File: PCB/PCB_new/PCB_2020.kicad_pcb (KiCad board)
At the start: 2 copper layers, 94 x 98.4 mm, 26 parts, among them IC1 LM358N, J1 TI_CONN, J10 SERVO_CONN, J11 MC_CONN, Q1 220mA/50V/3.5Ω, Q2 100V/17A, Q3 100V/17A, Q4 100V/17A, Q5 100V/17A, Q6 100V/17A

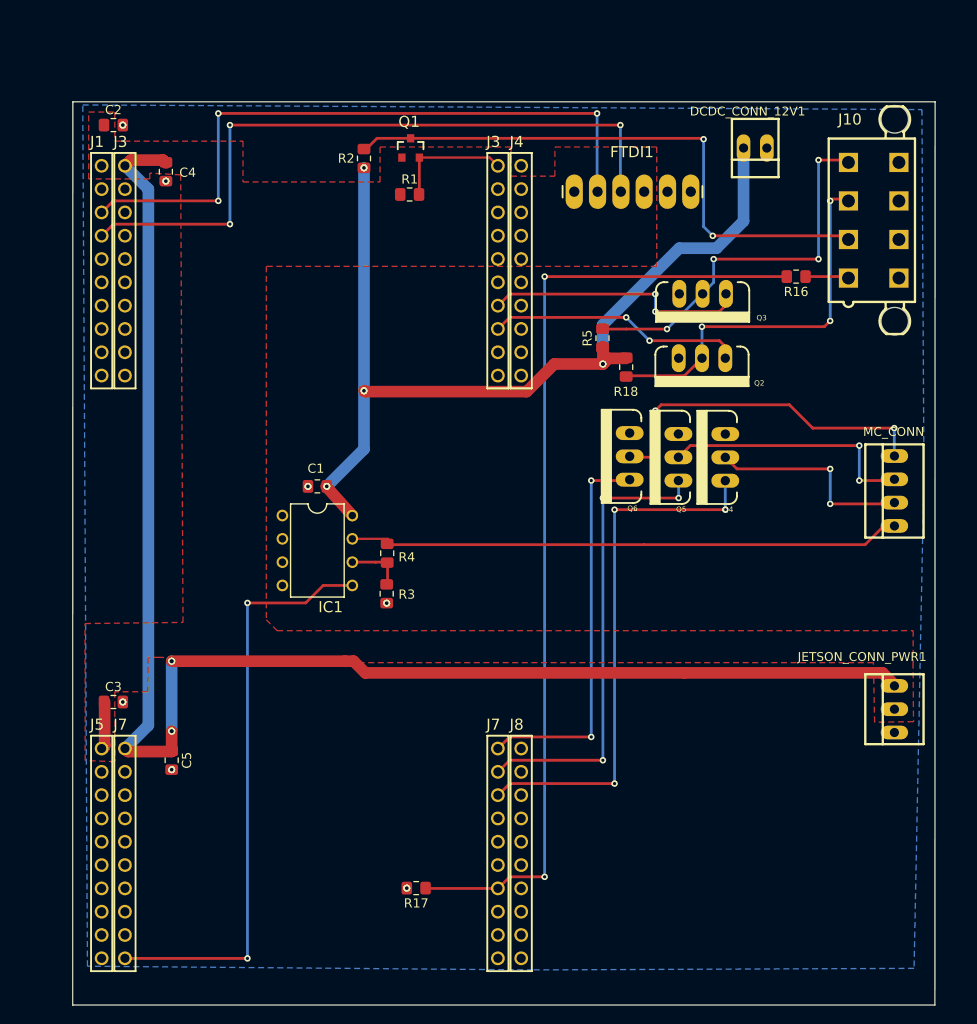
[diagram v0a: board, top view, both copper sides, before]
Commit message: new pcb design (still no braking signals)
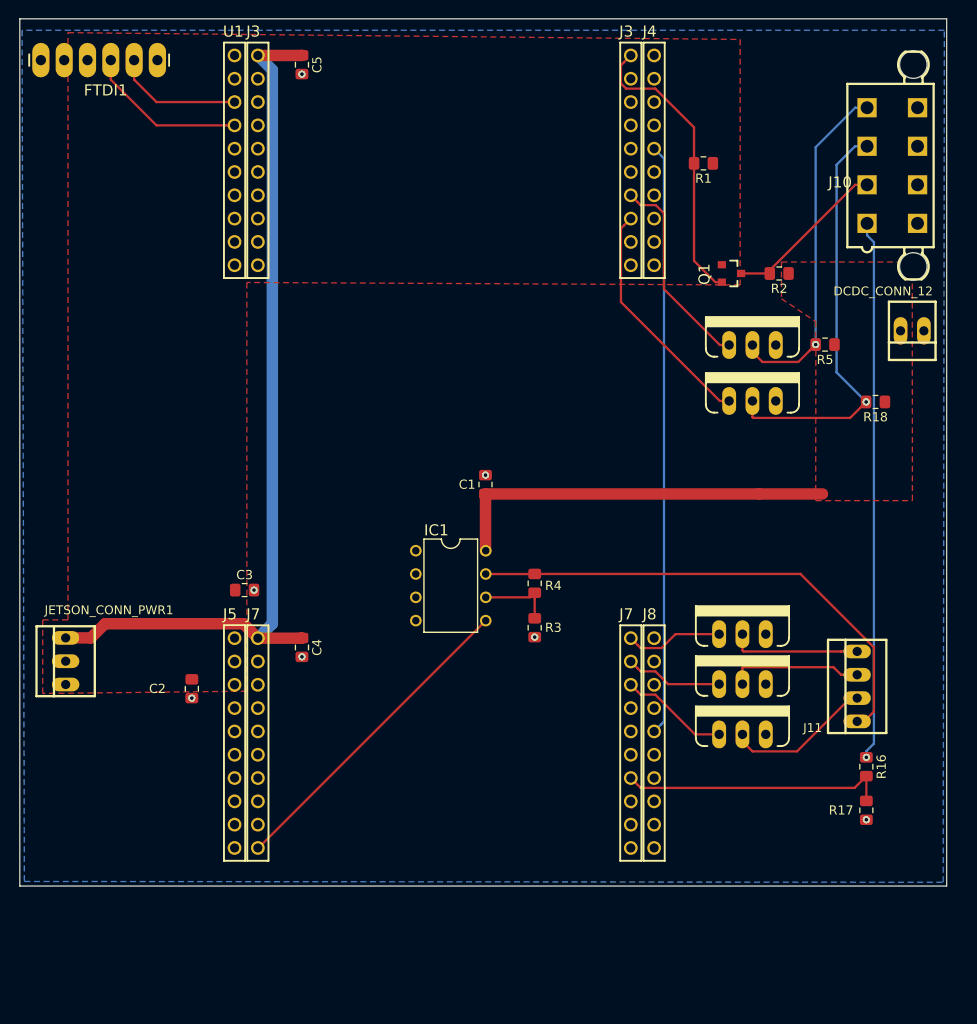
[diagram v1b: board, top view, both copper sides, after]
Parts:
- removed DCDC_CONN_12V1: 22-23-2021, Drivetrain_control:22-23-2021
- removed J1: TI_CONN, Drivetrain_control:TI_Footprint
- added DCDC_CONN_12: 22-23-2021, Drivetrain_control:22-23-2021, F.Cu at (193.0, 80.8)
- added U1: TI_CONN, Drivetrain_control:TI_Footprint, F.Cu at (118.0, 75.0)
- moved JETSON_CONN_PWR1 90.5 mm to (100.8, 116.8)
- moved C5 77.1 mm to (126.5, 51.8)
- moved C2 62.0 mm to (114.5, 119.8), turned to 270 degrees
- moved FTDI1 59.9 mm to (110.8, 51.2)
- moved R16 54.0 mm to (188.0, 128.2), turned to 270 degrees
- moved C4 53.9 mm to (126.5, 115.2)
- moved R17 49.8 mm to (188.0, 133.0), turned to 270 degrees
- moved R2 46.9 mm to (178.5, 74.5), turned to 180 degrees
- moved Q1 37.5 mm to (173.2, 74.5), turned to 270 degrees
- moved R1 32.2 mm to (170.2, 62.5), turned to 180 degrees
- moved Q4 30.2 mm to (174.5, 124.7), turned to 0 degrees
- moved R18 27.4 mm to (189.0, 88.5), turned to 180 degrees
- moved Q5 25.7 mm to (174.5, 119.2), turned to 0 degrees
- moved R5 24.3 mm to (183.5, 82.2), turned to 180 degrees
- moved Q6 22.9 mm to (174.5, 113.8), turned to 0 degrees
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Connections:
- FTDI1 pad 1: GND -> (no net)
- FTDI1 pad 2: (no net) -> SCIB_RX
- FTDI1 pad 3: +3V3 -> SCIB_TX
- FTDI1 pad 4: SCIB_TX -> +3V3
- FTDI1 pad 5: SCIB_RX -> (no net)
- FTDI1 pad 6: (no net) -> GND
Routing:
- net MC_HLFB+: track 105.3 -> 29.3 mm, vias 2 -> 0
- net +5V: track 165.4 -> 96.7 mm
- net /LAUNCHXL-F28379D Headers/RESET: track 0.00 -> 64.4 mm
- net +12V: track 105.0 -> 42.9 mm, vias 4 -> 0
- net SCIB_RX: track 72.3 -> 14.1 mm, vias 3 -> 0
- net SCIB_TX: track 74.8 -> 17.7 mm, vias 3 -> 0
- net /LAUNCHXL-F28379D Breakout/HLFB+: track 4.56 -> 58.8 mm, vias 0 -> 1
- net REV_CTL: track 58.3 -> 11.9 mm, vias 3 -> 0
- net /LAUNCHXL-F28379D Breakout/INPUT_B+: track 63.1 -> 17.9 mm, vias 2 -> 0
- net FWD_CTL: track 50.7 -> 10.6 mm, vias 3 -> 0
- net FS1_CTL: track 43.1 -> 10.7 mm, vias 2 -> 0
- net THROTTLE_DAC: track 64.3 -> 35.1 mm, vias 2 -> 0
- net /LAUNCHXL-F28379D Breakout/FS1_MC: track 38.1 -> 14.3 mm, vias 3 -> 0
- net TI_PWM: track 13.0 -> 32.0 mm
- net /LAUNCHXL-F28379D Breakout/FWD_MC: track 27.8 -> 14.6 mm, vias 2 -> 0
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- added copper zone on F.Cu, net +12V
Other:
- board size 94 x 98.4 mm -> 101 x 94.5 mm
- net class Power added: clearance 0.2, trace_width 1.25, via_dia 0.8, via_drill 0.4

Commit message: removed erroneous hidden traces
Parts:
- CONN1: renamed from FTDI1; value CONN_06LONGPADS -> FTDI
- CONN3: renamed from DCDC_CONN_12; value 22-23-2021 -> DCDC_CONN
- CONN4: renamed from JETSON_CONN_PWR1; value 22-23-2031 -> JETSON_CONN_PWR
- renumbered J10 to CONN2
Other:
- board text added: "MC_CONN"

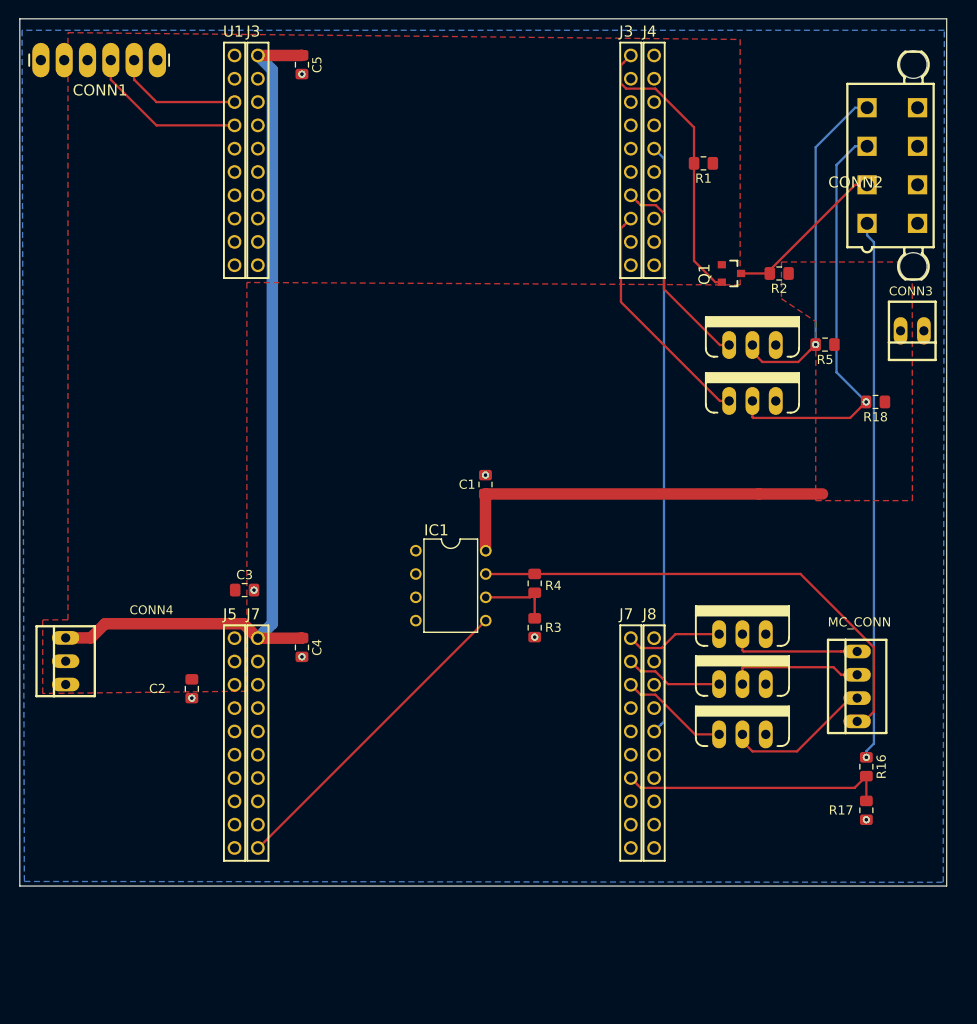
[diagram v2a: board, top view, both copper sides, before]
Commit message: fixed slight sizing issues
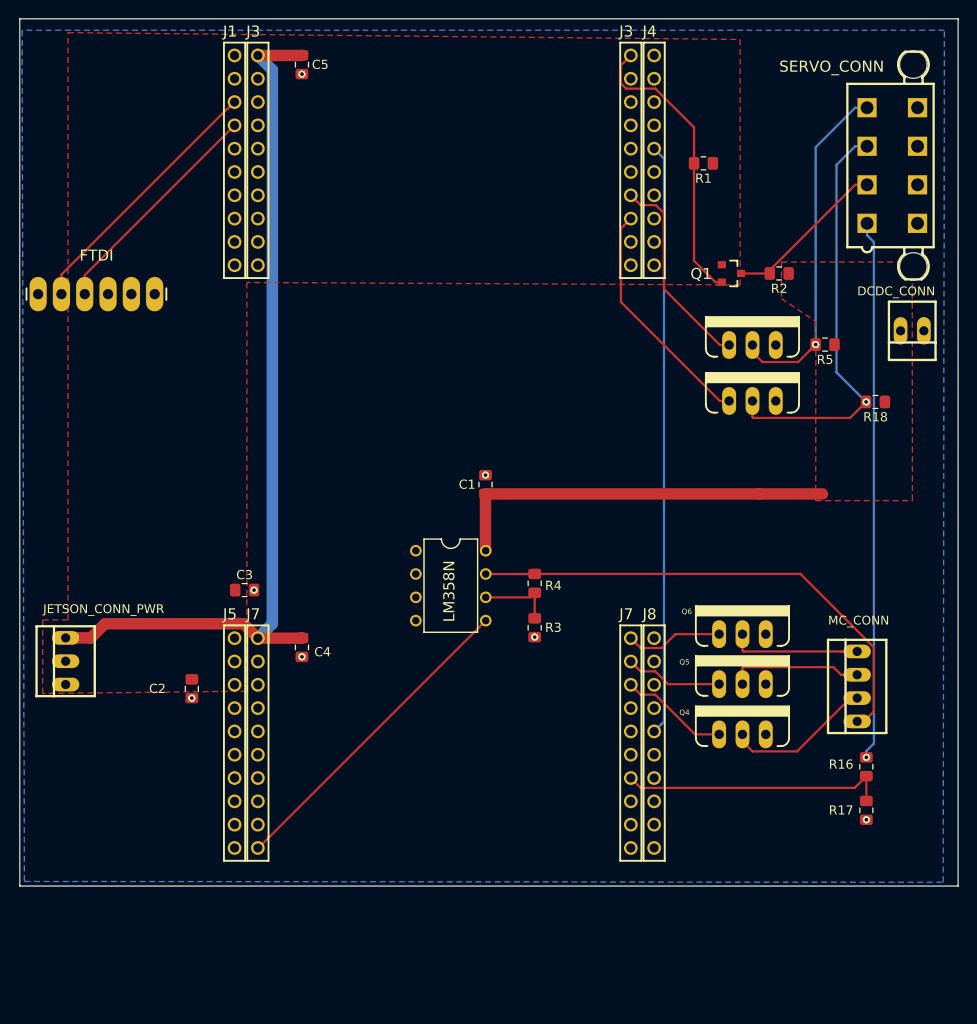
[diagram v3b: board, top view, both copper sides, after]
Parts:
- moved CONN1 28.6 mm to (97.8, 76.8), turned to 0 degrees
- renumbered J11 to CONN5, U1 to J1
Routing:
- net SCIB_RX: track 14.1 -> 28.8 mm
- net SCIB_TX: track 17.7 -> 25.2 mm
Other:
- board size 101 x 94.5 mm -> 102.2 x 94.5 mm
- board text removed: "MC_CONN"
